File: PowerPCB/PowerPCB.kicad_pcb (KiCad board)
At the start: 2 copper layers, 41 parts, among them J1 Conn_01x03_Male, J2 Conn_01x10_Male, J5 Conn_01x07_Male, K1 1721081-5, K2 1721081-5, K3 1721081-5, Q1 Q_PMOS_DGS, U1 NCP1117-3.3_SOT223, U2 STM32F413ZHTx, U3 NCP1117-5.0_SOT223, U4 MCP2562-E-P, U5 MCP2562-E-P

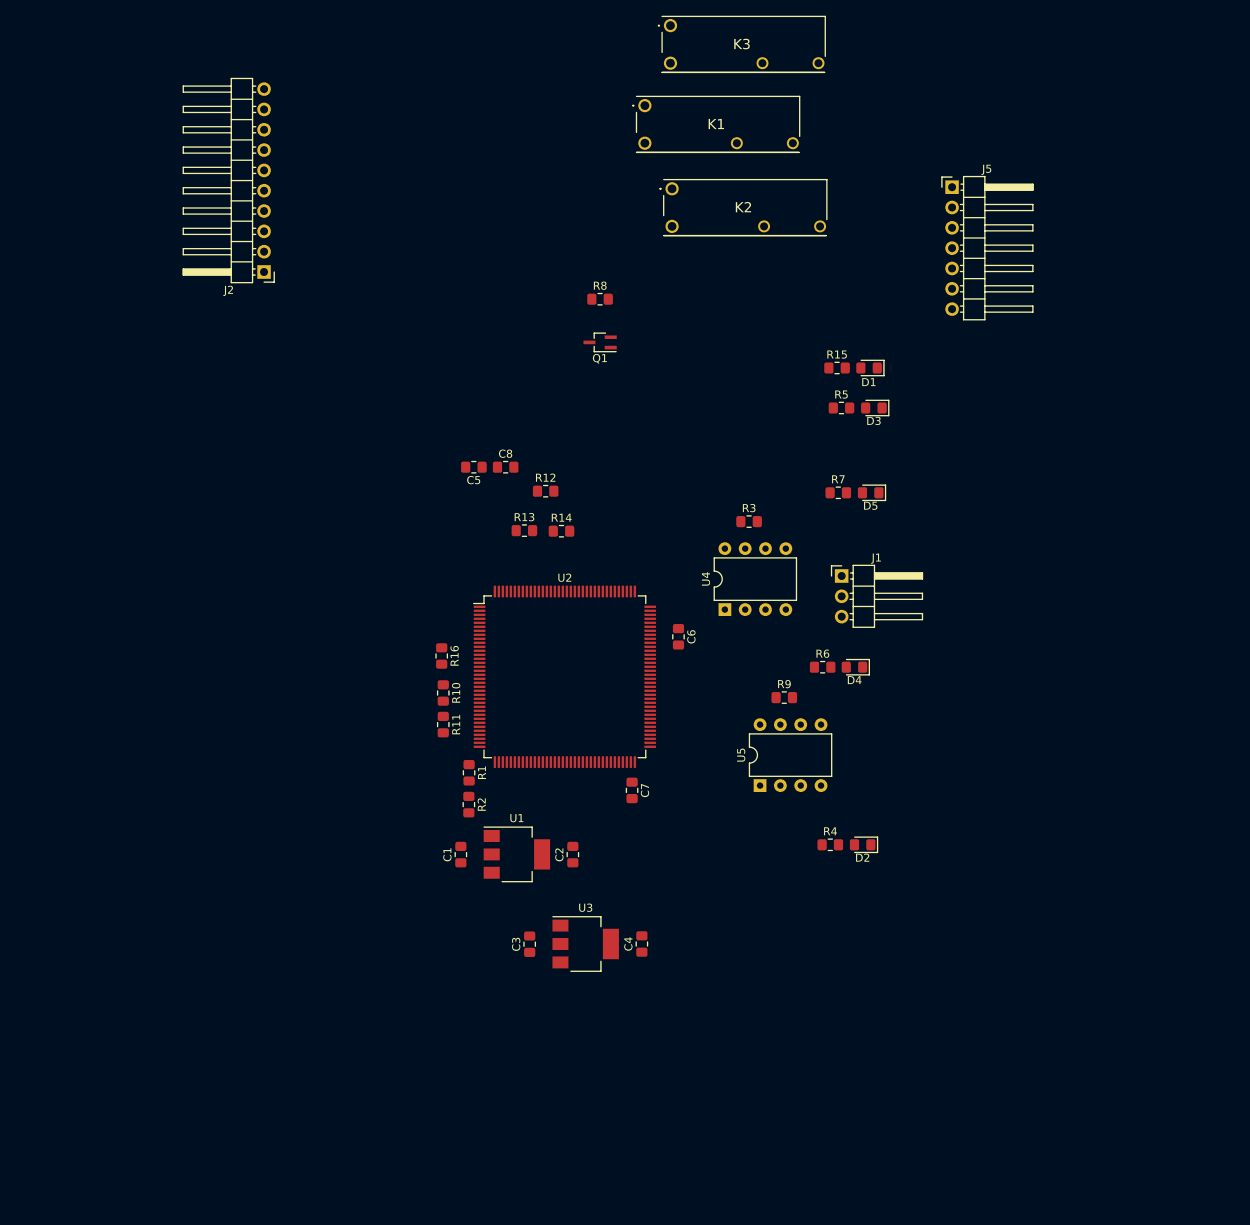
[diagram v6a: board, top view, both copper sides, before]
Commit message: UPdated PCB with protection
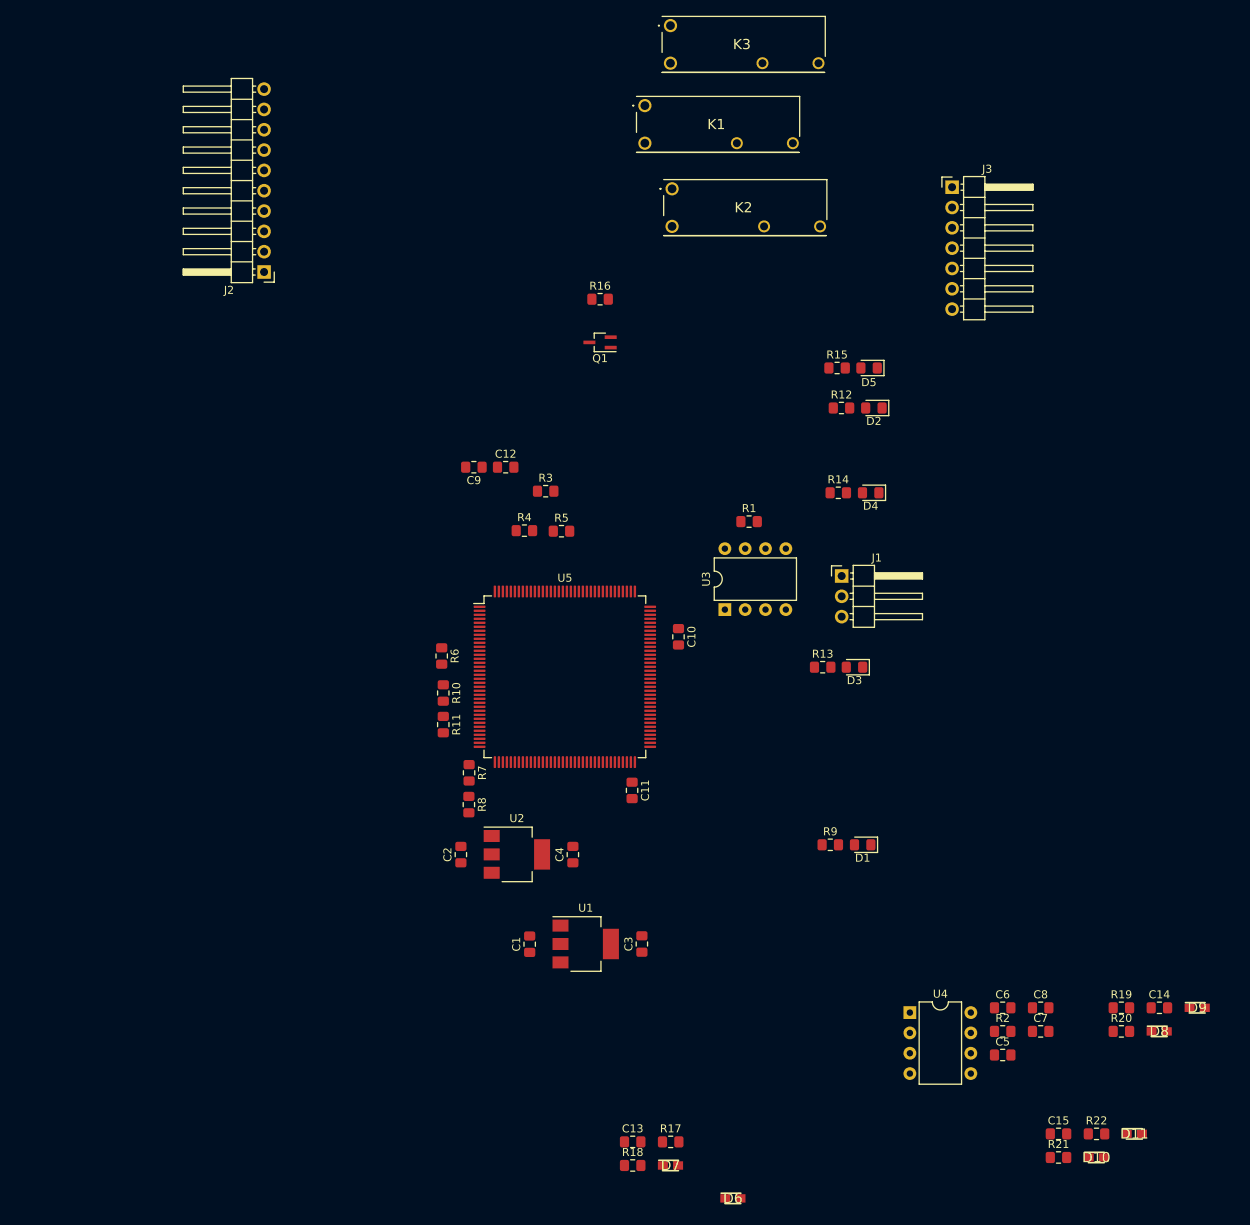
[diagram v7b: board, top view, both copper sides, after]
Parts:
- removed the R9 at (394.4, 216.6)
- removed the U5 at (391.4, 227.6)
- added C13: 10u, Capacitor_SMD:C_0805_2012Metric_Pad1.15x1.40mm_HandSolder, F.Cu at (375.5, 272.1)
- added C14: 10u, Capacitor_SMD:C_0805_2012Metric_Pad1.15x1.40mm_HandSolder, F.Cu at (441.3, 255.4)
- added C15: 10u, Capacitor_SMD:C_0805_2012Metric_Pad1.15x1.40mm_HandSolder, F.Cu at (428.7, 271.1)
- added C5: 0.1u, Capacitor_SMD:C_0805_2012Metric_Pad1.15x1.40mm_HandSolder, F.Cu at (421.7, 261.3)
- added C6: 0.1u, Capacitor_SMD:C_0805_2012Metric_Pad1.15x1.40mm_HandSolder, F.Cu at (421.7, 255.4)
- added C7: 0.1u, Capacitor_SMD:C_0805_2012Metric_Pad1.15x1.40mm_HandSolder, F.Cu at (426.5, 258.3)
- added C8: 0.1u, Capacitor_SMD:C_0805_2012Metric_Pad1.15x1.40mm_HandSolder, F.Cu at (426.5, 255.4)
- added D10: SD0805S040S0R1, SamacSys_Parts:DIOM2013X100N, F.Cu at (433.4, 274.1)
- added D11: SD0805S040S0R1, SamacSys_Parts:DIOM2013X100N, F.Cu at (438.2, 271.1)
- added D6: SD0805S040S0R1, SamacSys_Parts:DIOM2013X100N, F.Cu at (388.0, 279.2)
- added D7: SD0805S040S0R1, SamacSys_Parts:DIOM2013X100N, F.Cu at (380.2, 275.1)
- added D8: SD0805S040S0R1, SamacSys_Parts:DIOM2013X100N, F.Cu at (441.3, 258.3)
- added D9: SD0805S040S0R1, SamacSys_Parts:DIOM2013X100N, F.Cu at (446.0, 255.4)
- added R17: 10, Resistor_SMD:R_0805_2012Metric_Pad1.15x1.40mm_HandSolder, F.Cu at (380.2, 272.1)
- added R18: 1k, Resistor_SMD:R_0805_2012Metric_Pad1.15x1.40mm_HandSolder, F.Cu at (375.5, 275.1)
- added R19: 10, Resistor_SMD:R_0805_2012Metric_Pad1.15x1.40mm_HandSolder, F.Cu at (436.6, 255.4)
- added R2: 120, Resistor_SMD:R_0805_2012Metric_Pad1.15x1.40mm_HandSolder, F.Cu at (421.7, 258.3)
- added R20: 1k, Resistor_SMD:R_0805_2012Metric_Pad1.15x1.40mm_HandSolder, F.Cu at (436.6, 258.3)
- added R21: 10, Resistor_SMD:R_0805_2012Metric_Pad1.15x1.40mm_HandSolder, F.Cu at (428.7, 274.1)
- added R22: 1k, Resistor_SMD:R_0805_2012Metric_Pad1.15x1.40mm_HandSolder, F.Cu at (433.5, 271.1)
- added U4: MCP2562-E-P, Package_DIP:DIP-8_W7.62mm, F.Cu at (410.1, 256.0)
- C1: renamed from C3; value C -> 0.1u
- C2: renamed from C1; value C -> 0.1u
- C3: renamed from C4; value C -> 0.1u
- C4: renamed from C2; value C -> 0.1u
- renumbered C6 to C10, C7 to C11, C8 to C12, C5 to C9, D2 to D1, D3 to D2, D4 to D3, D5 to D4, D1 to D5, J5 to J3, R3 to R1, R5 to R12, R6 to R13, R7 to R14, R8 to R16, R12 to R3, R13 to R4, R14 to R5, R16 to R6, R1 to R7, R2 to R8, R4 to R9, U3 to U1, U1 to U2, U4 to U3, U2 to U5
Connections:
- R10 pad 2: Net-(R10-Pad2) -> /InputProtection3/Vin
- R11 pad 1: Net-(R10-Pad2) -> /InputProtection3/Vin
- R4 pad 2: Net-(R13-Pad2) -> /InputProtection/Vin
- R5 pad 1: Net-(R13-Pad2) -> /InputProtection/Vin
- R7 pad 2: Net-(R1-Pad2) -> /InputProtection2/Vin
- R8 pad 1: Net-(R1-Pad2) -> /InputProtection2/Vin
- U5 pad 124: Net-(R13-Pad2) -> /InputProtection/ToSTM
- U5 pad 26: Net-(R10-Pad2) -> /InputProtection3/ToSTM
- U5 pad 37: Net-(R1-Pad2) -> /InputProtection2/ToSTM

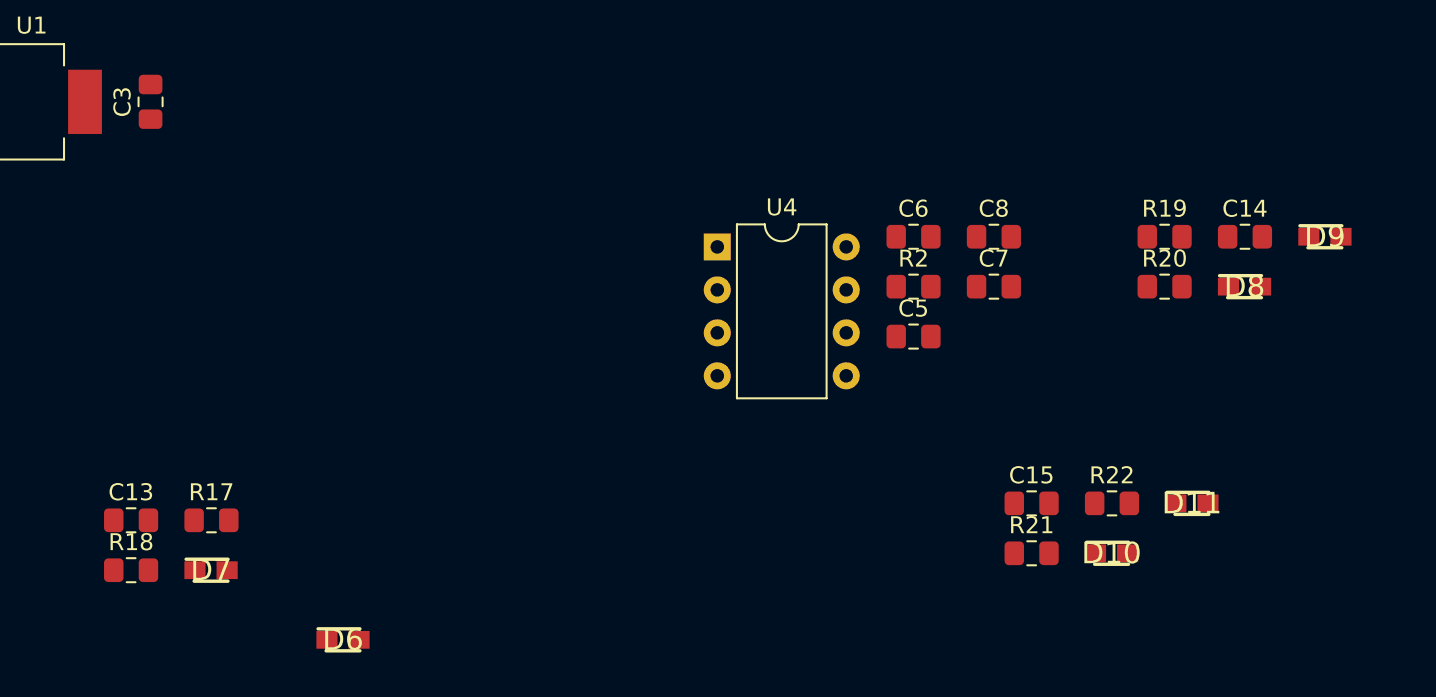
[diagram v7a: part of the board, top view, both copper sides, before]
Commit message: diode labels look nicer
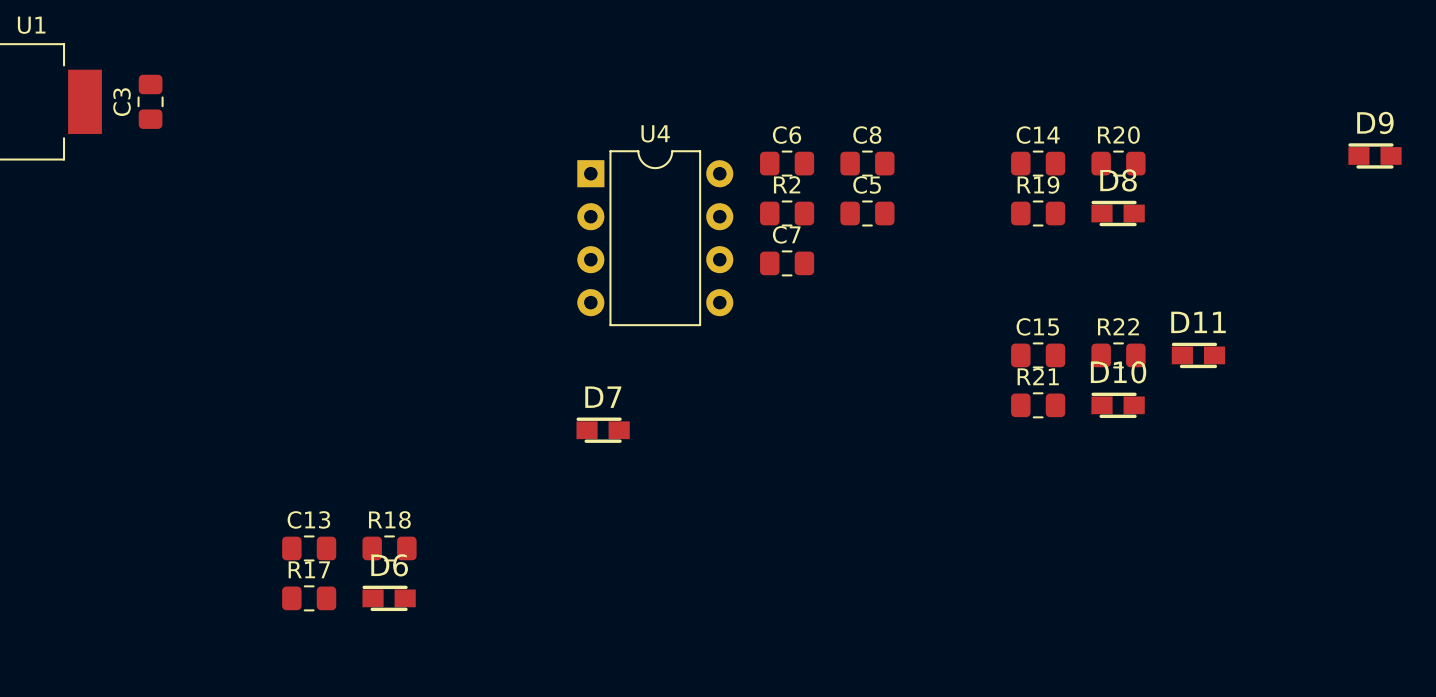
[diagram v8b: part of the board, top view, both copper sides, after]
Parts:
- moved D7 24.6 mm to (403.4, 266.8)
- moved R18 15.3 mm to (390.8, 273.8)
- moved C14 13.0 mm to (429.1, 251.1)
- moved C7 12.3 mm to (414.2, 256.9)
- moved C13 10.7 mm to (386.0, 273.8)
- moved C15 8.75 mm to (429.1, 262.4)
- moved D10 8.75 mm to (433.8, 265.3)
- moved D11 8.75 mm to (438.6, 262.4)
- moved R21 8.75 mm to (429.1, 265.3)
- moved R22 8.75 mm to (433.8, 262.4)
- moved C6 8.64 mm to (414.2, 251.1)
- moved C8 8.64 mm to (419.0, 251.1)
- moved D8 8.64 mm to (433.8, 254.0)
- moved R2 8.64 mm to (414.2, 254.0)
- moved U4 8.64 mm to (402.6, 251.7)
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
